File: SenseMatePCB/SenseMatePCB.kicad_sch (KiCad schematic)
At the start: 16 parts, among them M1 Motor_DC, Q1 2SC1815, Q2 2SC1815, SW1 SW_Push, SW2 SW_Push, SW3 SW_Push, SW5 SW_DPDT_x2

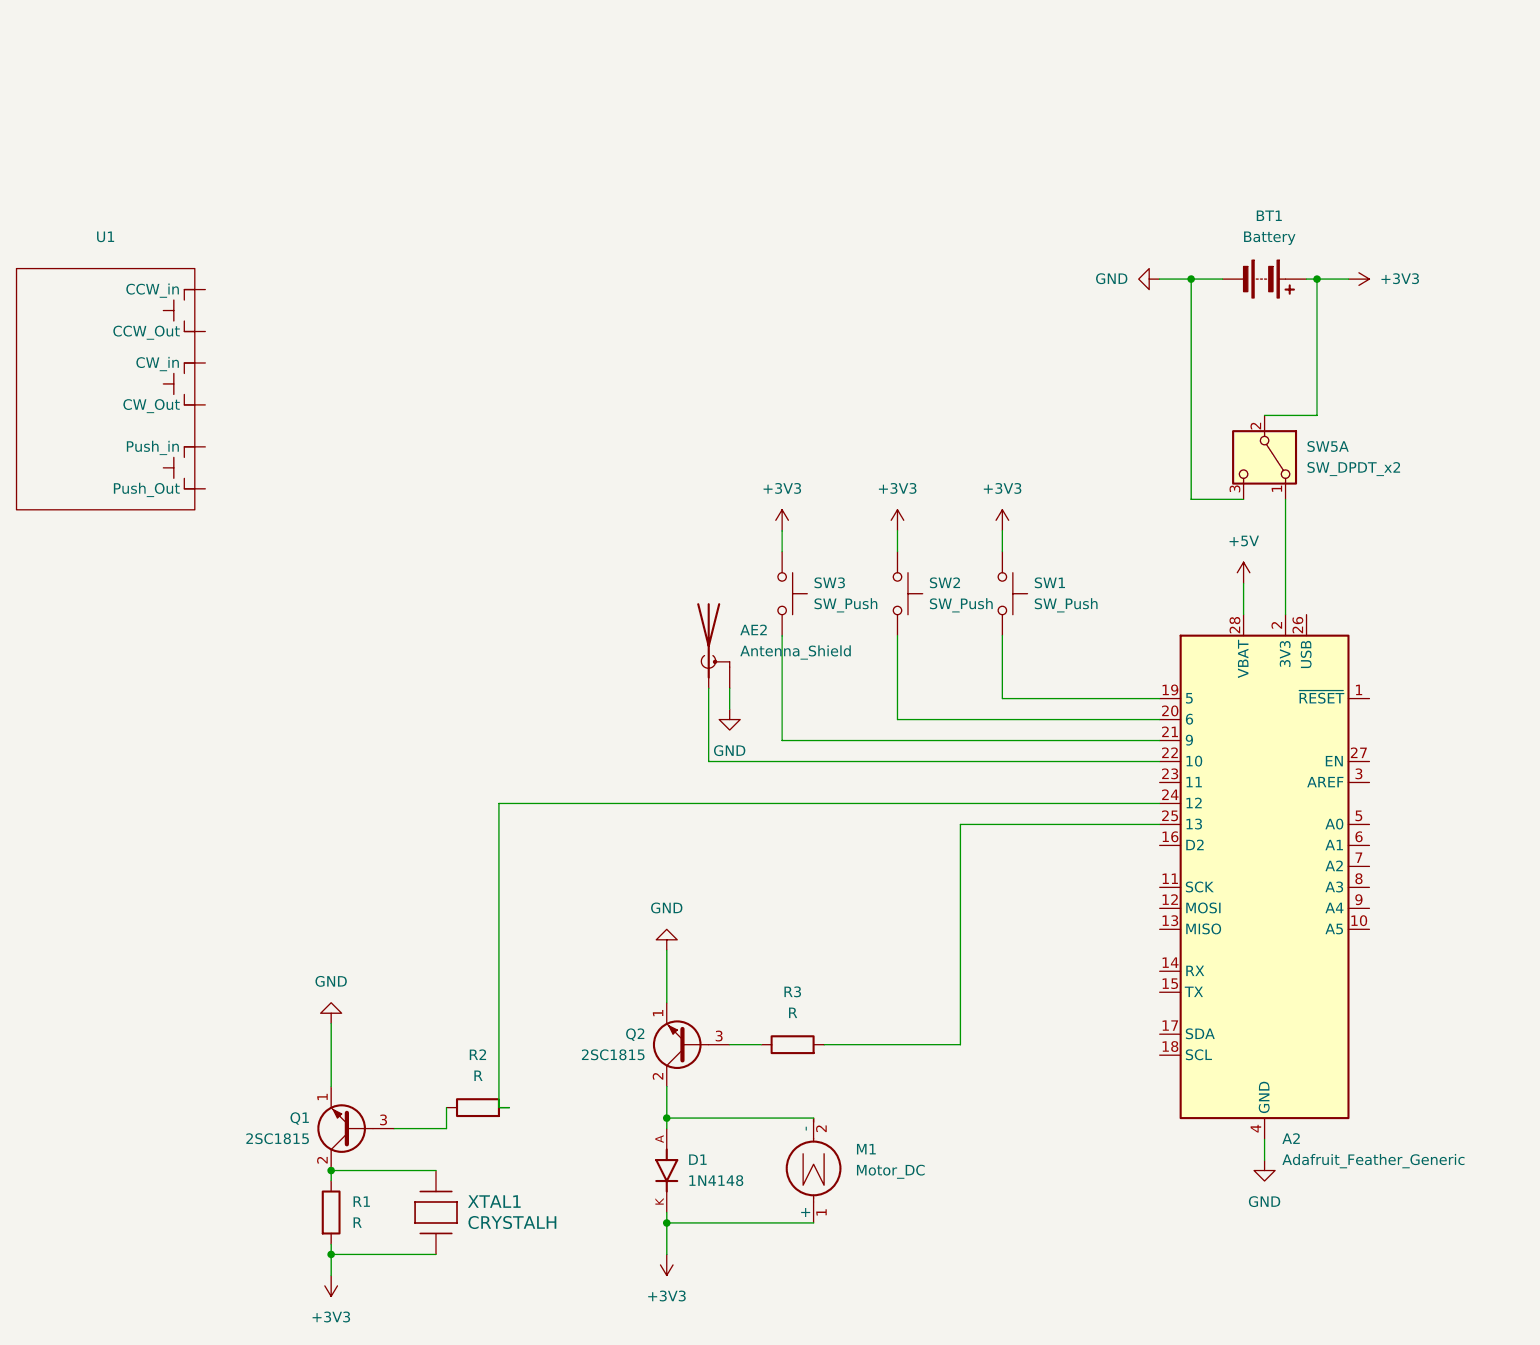
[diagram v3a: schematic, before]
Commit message: changed the button to own implementation
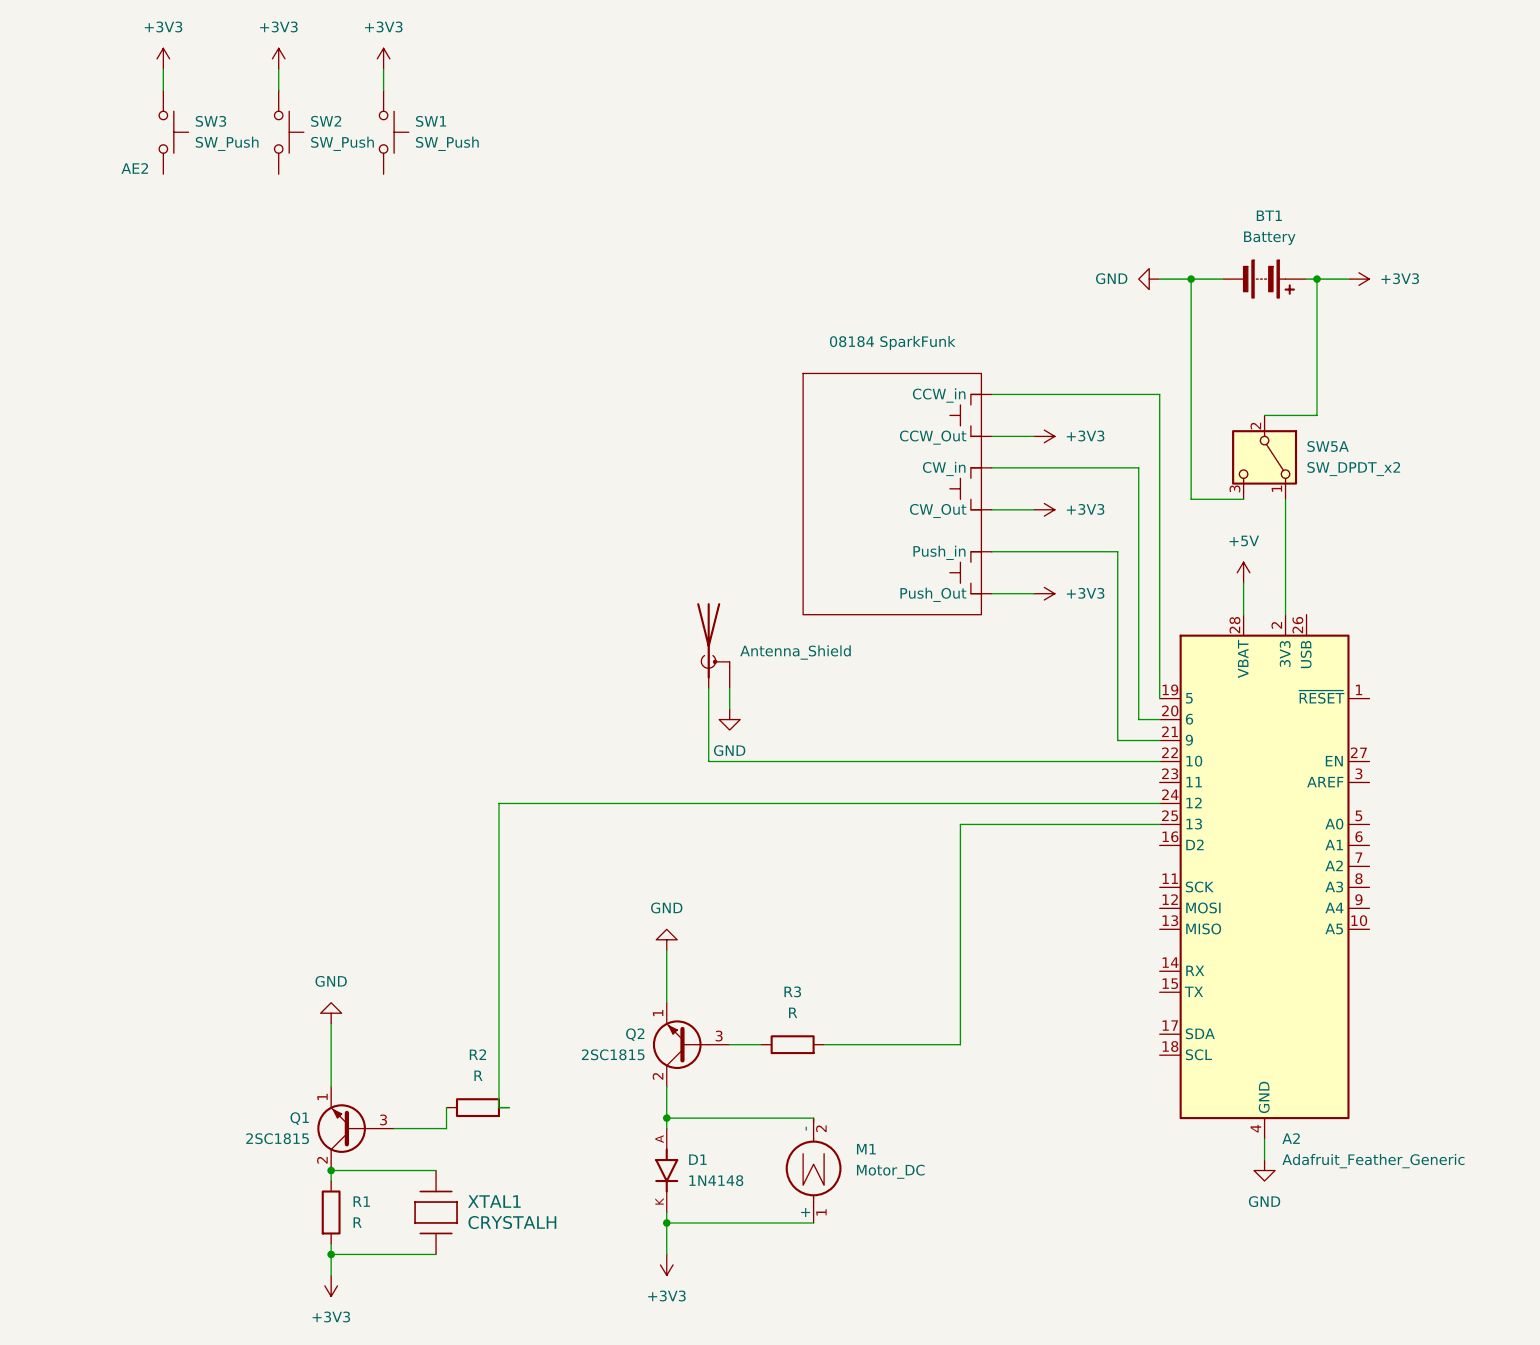
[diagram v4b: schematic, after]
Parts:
- 08184 SparkFunk: renamed from U1
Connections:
- net +3V3: now also 08184 SparkFunk. (Push_Out)
- net at A2.21 (9): now also 08184 SparkFunk. (Push_Out); no longer SW3.2
- net at A2.19 (5): now also 08184 SparkFunk. (Push_Out); no longer SW1.2
- net at A2.20 (6): now also 08184 SparkFunk. (Push_Out); no longer SW2.2
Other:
- moved on the sheet: 08184 SparkFunk, SW1, SW2, SW3
